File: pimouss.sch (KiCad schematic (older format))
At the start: 18 parts, among them J1 Conn_02x10_Odd_Even, J2 TMS-105-57-GD, J3 Conn_02x10_Odd_Even, P1 QSH-060-01-L-D-A, U1 SN74AUC1G19

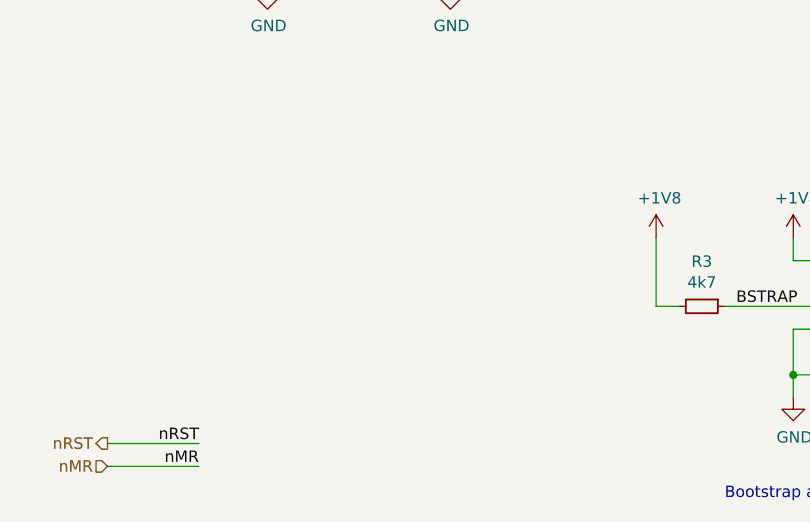
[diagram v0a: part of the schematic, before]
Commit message: sch, master: Add pimouss SoM component
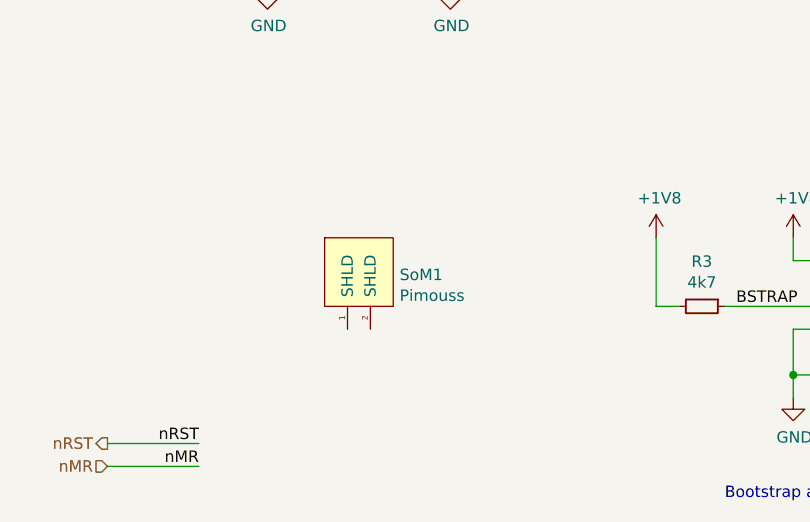
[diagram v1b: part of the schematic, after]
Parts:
- added SoM1: Pimouss, pimouss-motherboard:Pimouss, symbol pimouss-motherboard:Pimouss
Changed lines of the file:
@@
 	3000 1800 3400 1800
 Connection ~ 7100 4400
+$Comp
+L pimouss-motherboard:Pimouss SoM1
+U 1 1 5DBDBE10
+P 2450 5700
+F 0 "SoM1" H 2778 5538 50  0000 L CNN
+F 1 "Pimouss" H 2778 5447 50  0000 L CNN
+F 2 "pimouss-motherboard:Pimouss" H 2450 5700 50  0001 C CNN
+F 3 "" H 2450 5700 50  0001 C CNN
+	1    2450 5700
+	1    0    0    -1
+$EndComp
 $EndSCHEMATC

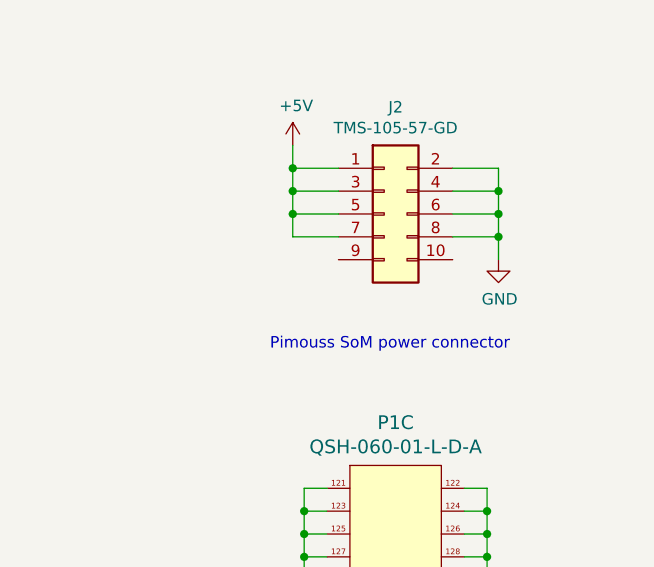
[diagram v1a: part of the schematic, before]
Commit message: lib: Finally fix TSM-105 symbol
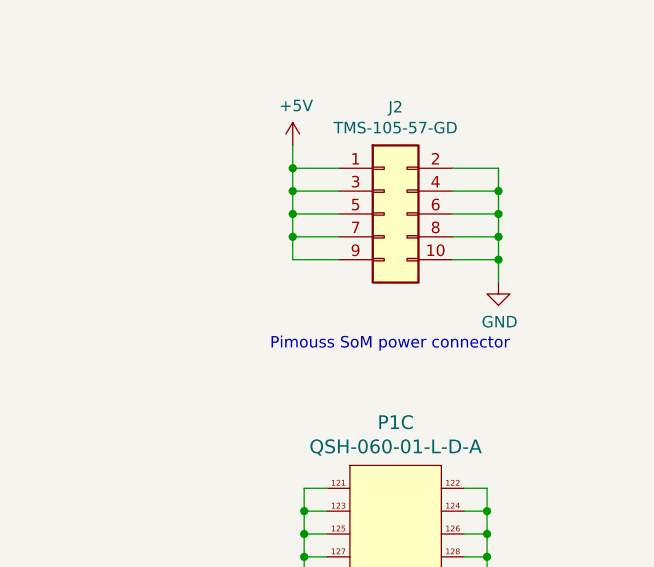
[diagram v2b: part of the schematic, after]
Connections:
- net +5V: now also J2.9 (Pin_9)
- net GND: now also J2.10 (Pin_10)
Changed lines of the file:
@@
 L power:GND #PWR025
 U 1 1 5DAB4CAB
-P 10350 2550
-F 0 "#PWR025" H 10350 2300 50  0001 C CNN
-F 1 "GND" H 10355 2377 50  0000 C CNN
-F 2 "" H 10350 2550 50  0001 C CNN
-F 3 "" H 10350 2550 50  0001 C CNN
-	1    10350 2550
+P 10350 2650
+F 0 "#PWR025" H 10350 2400 50  0001 C CNN
+F 1 "GND" H 10355 2477 50  0000 C CNN
+F 2 "" H 10350 2650 50  0001 C CNN
+F 3 "" H 10350 2650 50  0001 C CNN
+	1    10350 2650
 	1    0    0    -1
 $EndComp
@@
 	10150 2450 10350 2450
 Connection ~ 10350 2450
-Wire Wire Line
-	10350 2450 10350 2550
 Text Notes 10400 2950 2    50   ~ 0
 Pimouss SoM power connector
@@
 	1    0    0    -1
 $EndComp
+Wire Wire Line
+	10350 2450 10350 2550
+Wire Wire Line
+	10150 2550 10350 2550
+Connection ~ 10350 2550
+Wire Wire Line
+	10350 2550 10350 2650
+Wire Wire Line
+	9650 2550 9450 2550
+Wire Wire Line
+	9450 2550 9450 2450
+Connection ~ 9450 2450
 $EndSCHEMATC

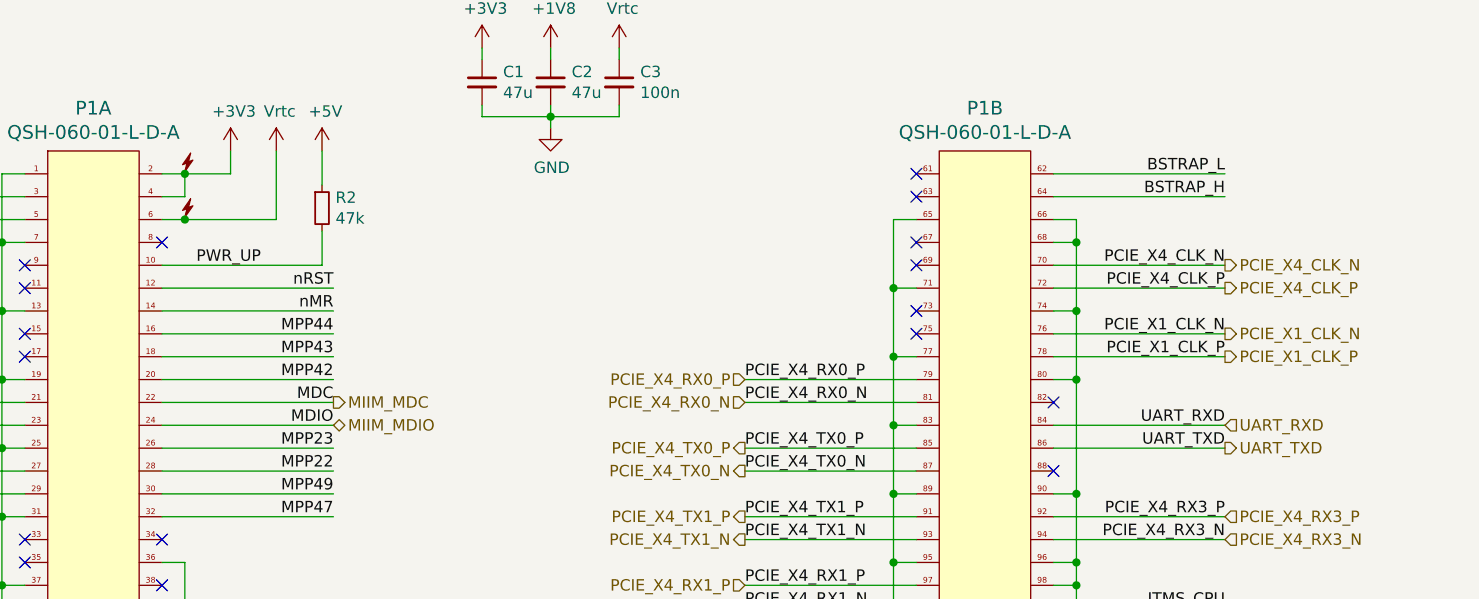
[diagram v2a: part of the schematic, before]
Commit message: sch, pcb: Add testpads on lots of signals
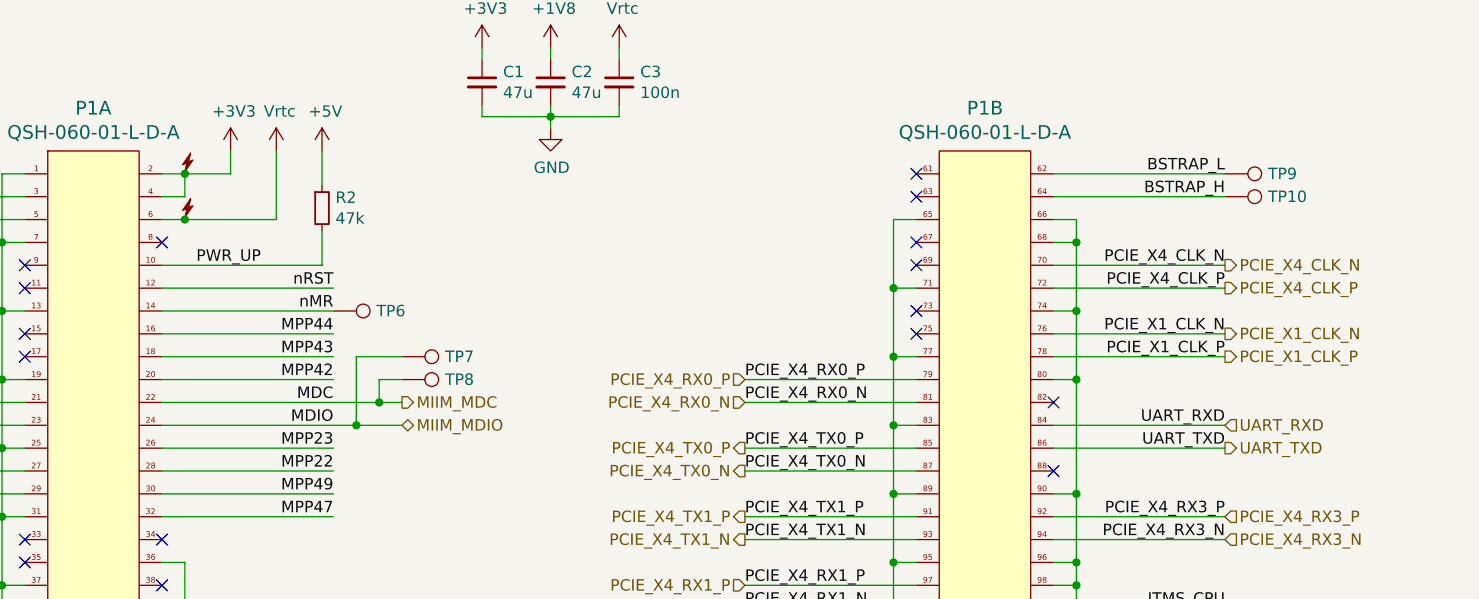
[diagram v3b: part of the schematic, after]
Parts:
- added TP10, TP6, TP7, TP8, TP9: TestPoint, TestPoint:TestPoint_Pad_D1.0mm, symbol Connector:TestPoint
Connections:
- net BSTRAP_H: now also TP10.1
- net BSTRAP_L: now also TP9.1
- net MIIM_MDC: now also TP8.1
- net MIIM_MDIO: now also TP7.1
- net nMR: now also TP6.1
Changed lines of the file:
@@
 PCIE_X4_RX3_N
-Wire Wire Line
-	3650 2600 2900 2600
-Wire Wire Line
-	3650 2700 2900 2700
 Wire Wire Line
 	3650 2100 2900 2100
@@
 NoConn ~ 6200 2200
 NoConn ~ 6200 2300
-Wire Wire Line
-	7550 1600 6800 1600
-Wire Wire Line
-	7550 1700 6800 1700
-Text Label 7550 1600 2    50   ~ 0
-BSTRAP_L
-Text Label 7550 1700 2    50   ~ 0
-BSTRAP_H
 NoConn ~ 6800 2900
 NoConn ~ 6800 2600
@@
 Text HLabel 3650 4500 2    50   BiDi ~ 0
 SD_D0
-Text HLabel 3650 2600 2    50   Output ~ 0
+Text HLabel 3950 2600 2    50   Output ~ 0
 MIIM_MDC
-Text HLabel 3650 2700 2    50   BiDi ~ 0
+Text HLabel 3950 2700 2    50   BiDi ~ 0
 MIIM_MDIO
 Text HLabel 1550 1800 0    50   Output ~ 0
@@
 	9450 2550 9450 2450
 Connection ~ 9450 2450
+$Comp
+L Connector:TestPoint TP?
+U 1 1 5D19D3D1
+P 3950 2400
+AR Path="/5D05A5E1/5D19D3D1" Ref="TP?"  Part="1"
+AR Path="/5CE77C37/5D19D3D1" Ref="TP7"  Part="1"
+F 0 "TP7" V 3950 2588 50  0000 L CNN
+F 1 "TestPoint" V 3995 2588 50  0001 L CNN
+F 2 "TestPoint:TestPoint_Pad_D1.0mm" H 4150 2400 50  0001 C CNN
+F 3 "~" H 4150 2400 50  0001 C CNN
+	1    3950 2400
+	0    1    1    0
+$EndComp
+$Comp
+L Connector:TestPoint TP?
+U 1 1 5D1B314D
+P 3950 2500
+AR Path="/5D05A5E1/5D1B314D" Ref="TP?"  Part="1"
+AR Path="/5CE77C37/5D1B314D" Ref="TP8"  Part="1"
+F 0 "TP8" V 3950 2688 50  0000 L CNN
+F 1 "TestPoint" V 3995 2688 50  0001 L CNN
+F 2 "TestPoint:TestPoint_Pad_D1.0mm" H 4150 2500 50  0001 C CNN
+F 3 "~" H 4150 2500 50  0001 C CNN
+	1    3950 2500
+	0    1    1    0
+$EndComp
+Wire Wire Line
+	2900 2600 3850 2600
+Wire Wire Line
+	2900 2700 3750 2700
+Wire Wire Line
+	3950 2500 3850 2500
+Wire Wire Line
+	3850 2500 3850 2600
+Connection ~ 3850 2600
+Wire Wire Line
+	3850 2600 3950 2600
+Wire Wire Line
+	3950 2400 3750 2400
+Wire Wire Line
+	3750 2400 3750 2700
+Connection ~ 3750 2700
+Wire Wire Line
+	3750 2700 3950 2700
+Text Label 7550 1700 2    50   ~ 0
+BSTRAP_H
+Text Label 7550 1600 2    50   ~ 0
+BSTRAP_L
+Wire Wire Line
+	7550 1600 6800 1600
+Wire Wire Line
+	7550 1700 6800 1700
+$Comp
+L Connector:TestPoint TP?
+U 1 1 5D2A7F76
+P 7550 1600
+AR Path="/5D05A5E1/5D2A7F76" Ref="TP?"  Part="1"
+AR Path="/5CE77C37/5D2A7F76" Ref="TP9"  Part="1"
+F 0 "TP9" V 7550 1788 50  0000 L CNN
+F 1 "TestPoint" V 7595 1788 50  0001 L CNN
+F 2 "TestPoint:TestPoint_Pad_D1.0mm" H 7750 1600 50  0001 C CNN
+F 3 "~" H 7750 1600 50  0001 C CNN
+	1    7550 1600
+	0    1    1    0
+$EndComp
+$Comp
+L Connector:TestPoint TP?
+U 1 1 5D2A76E3
+P 7550 1700
+AR Path="/5D05A5E1/5D2A76E3" Ref="TP?"  Part="1"
+AR Path="/5CE77C37/5D2A76E3" Ref="TP10"  Part="1"
+F 0 "TP10" V 7550 1888 50  0000 L CNN
+F 1 "TestPoint" V 7595 1888 50  0001 L CNN
+F 2 "TestPoint:TestPoint_Pad_D1.0mm" H 7750 1700 50  0001 C CNN
+F 3 "~" H 7750 1700 50  0001 C CNN
+	1    7550 1700
+	0    1    1    0
+$EndComp
+$Comp
+L Connector:TestPoint TP?
+U 1 1 5D3350DF
+P 3650 2200
+AR Path="/5D05A5E1/5D3350DF" Ref="TP?"  Part="1"
+AR Path="/5CE77C37/5D3350DF" Ref="TP6"  Part="1"
+F 0 "TP6" V 3650 2388 50  0000 L CNN
+F 1 "TestPoint" V 3695 2388 50  0001 L CNN
+F 2 "TestPoint:TestPoint_Pad_D1.0mm" H 3850 2200 50  0001 C CNN
+F 3 "~" H 3850 2200 50  0001 C CNN
+	1    3650 2200
+	0    1    1    0
+$EndComp
 $EndSCHEMATC

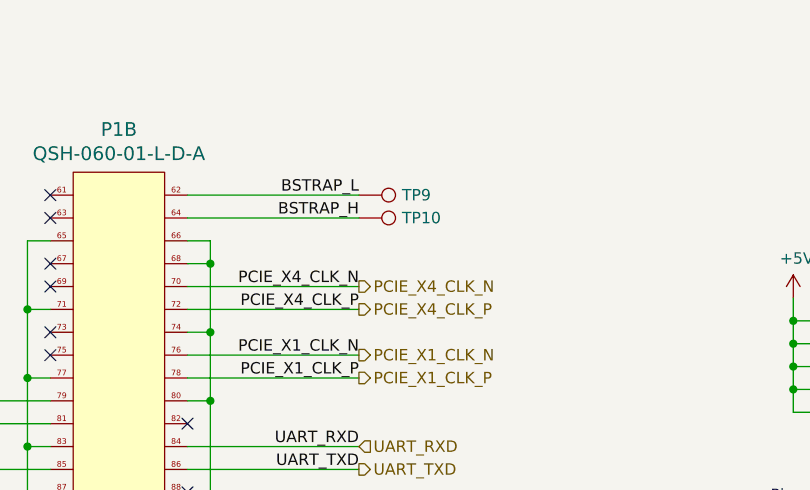
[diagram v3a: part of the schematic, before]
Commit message: sch: Remove BSTRAP_H/L test pads
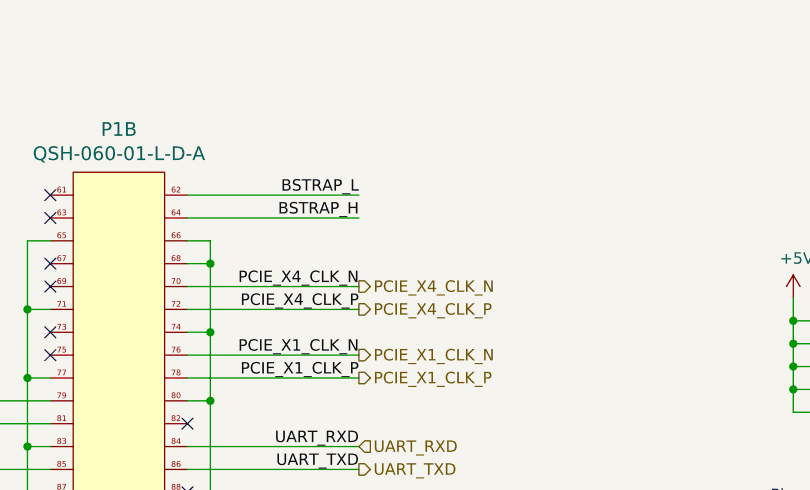
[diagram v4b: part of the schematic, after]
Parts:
- removed TP10, TP9: TestPoint, TestPoint:TestPoint_Pad_D1.0mm, symbol Connector:TestPoint
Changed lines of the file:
@@
-$Comp
-L Connector:TestPoint TP?
-U 1 1 5D2A7F76
-P 7550 1600
-AR Path="/5D05A5E1/5D2A7F76" Ref="TP?"  Part="1"
-AR Path="/5CE77C37/5D2A7F76" Ref="TP9"  Part="1"
-F 0 "TP9" V 7550 1788 50  0000 L CNN
-F 1 "TestPoint" V 7595 1788 50  0001 L CNN
-F 2 "TestPoint:TestPoint_Pad_D1.0mm" H 7750 1600 50  0001 C CNN
-F 3 "~" H 7750 1600 50  0001 C CNN
-	1    7550 1600
-	0    1    1    0
-$EndComp
-$Comp
-L Connector:TestPoint TP?
-U 1 1 5D2A76E3
-P 7550 1700
-AR Path="/5D05A5E1/5D2A76E3" Ref="TP?"  Part="1"
-AR Path="/5CE77C37/5D2A76E3" Ref="TP10"  Part="1"
-F 0 "TP10" V 7550 1888 50  0000 L CNN
-F 1 "TestPoint" V 7595 1888 50  0001 L CNN
-F 2 "TestPoint:TestPoint_Pad_D1.0mm" H 7750 1700 50  0001 C CNN
-F 3 "~" H 7750 1700 50  0001 C CNN
-	1    7550 1700
-	0    1    1    0
-$EndComp
 $Comp
 L Connector:TestPoint TP?

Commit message: sch, pcb: Replace CH340 with FT230 and add USB host port
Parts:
- added P6: USB-C-2.0-FEMALE, pimouss-motherboard:USB-C-FEMALE, symbol pimouss-motherboard:USB-C-2.0-FEMALE
- added R82, R83: 56k, Resistor_SMD:R_0603_1608Metric, symbol Device:R_Small
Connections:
- net +5V: now also P6.A4 (VBUS), P6.A9 (VBUS), P6.B4 (VBUS), P6.B9 (VBUS), R82.2, R83.2
- net GND: now also P6.A1 (GND), P6.A12 (GND), P6.B1 (GND), P6.B12 (GND), P6.S1 (SHIELD), P6.S2 (SHIELD), P6.S3 (SHIELD), P6.S4 (SHIELD)
- net USB_HOST_N: now reaches P1.38
- net USB_HOST_N: now also P6.A7 (D-), P6.B7 (D-)
- net USB_HOST_P: now reaches P1.40
- net USB_HOST_P: now also P6.A6 (D+), P6.B6 (D+)
- new net: P6.A5 (CC1), R82.1
- new net: P6.B5 (CC2), R83.1
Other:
- moved on the sheet: J2, P1C

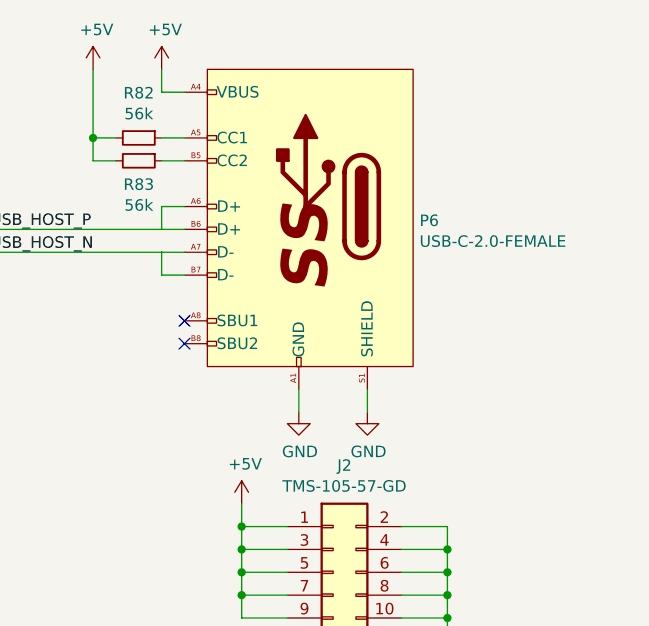
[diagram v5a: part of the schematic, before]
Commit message: sch, pcb: Replace USB-C connectors with vertical ones
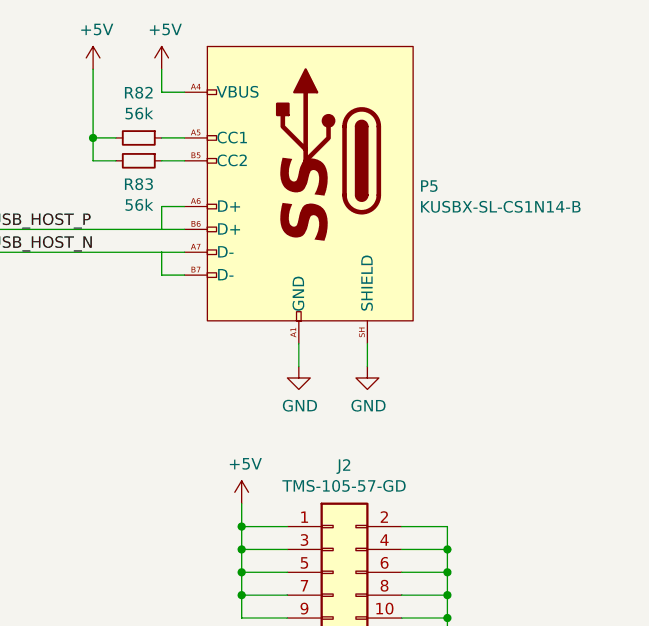
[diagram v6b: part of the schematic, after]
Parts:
- removed P6: USB-C-2.0-FEMALE, pimouss-motherboard:USB-C-FEMALE, symbol pimouss-motherboard:USB-C-2.0-FEMALE
- added P5: KUSBX-SL-CS1N14-B, pimouss-motherboard:KUSBX-SL-CS1N14-B, symbol pimouss-motherboard:KUSBX-SL-CS1N14-B
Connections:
- net +5V: now also P5.A4 (VBUS), P5.A9 (VBUS), P5.B4 (VBUS), P5.B9 (VBUS)
- net GND: now also P5.A1 (GND), P5.A12 (GND), P5.B1 (GND), P5.B12 (GND), P5.SH (SHIELD)
- net USB_HOST_N: now also P5.A7 (D-), P5.B7 (D-)
- net USB_HOST_P: now also P5.A6 (D+), P5.B6 (D+)
- net at R82.1: now also P5.A5 (CC1)
- net at R83.1: now also P5.B5 (CC2)
- no-connect marks 28 -> 26
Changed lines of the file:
@@
 Text Label 3650 3500 2    50   ~ 0
 USB_HOST_P
-$Comp
-L pimouss-motherboard:USB-C-2.0-FEMALE P6
-U 1 1 5DDF3054
-P 10400 750
-F 0 "P6" H 10372 88  50  0000 R CNN
-F 1 "USB-C-2.0-FEMALE" H 10372 -3  50  0000 R CNN
-F 2 "pimouss-motherboard:USB-C-FEMALE" H 11150 -750 50  0001 C CNN
-F 3 "https://www.usb.org/sites/default/files/documents/usb_type-c.zip" H 11050 250 50  0001 C CNN
-	1    10400 750
-	-1   0    0    -1
-$EndComp
 Text Label 1900 6700 2    50   ~ 0
 nMR
@@
 L power:GND #PWR0160
 U 1 1 5DED3B57
-P 9900 2250
-F 0 "#PWR0160" H 9900 2000 50  0001 C CNN
-F 1 "GND" H 9905 2077 50  0000 C CNN
-F 2 "" H 9900 2250 50  0001 C CNN
-F 3 "" H 9900 2250 50  0001 C CNN
-	1    9900 2250
+P 9900 2050
+F 0 "#PWR0160" H 9900 1800 50  0001 C CNN
+F 1 "GND" H 9905 1877 50  0000 C CNN
+F 2 "" H 9900 2050 50  0001 C CNN
+F 3 "" H 9900 2050 50  0001 C CNN
+	1    9900 2050
 	1    0    0    -1
 $EndComp
@@
 L power:GND #PWR0195
 U 1 1 5DED4037
-P 10200 2250
-F 0 "#PWR0195" H 10200 2000 50  0001 C CNN
-F 1 "GND" H 10205 2077 50  0000 C CNN
-F 2 "" H 10200 2250 50  0001 C CNN
-F 3 "" H 10200 2250 50  0001 C CNN
-	1    10200 2250
+P 10200 2050
+F 0 "#PWR0195" H 10200 1800 50  0001 C CNN
+F 1 "GND" H 10205 1877 50  0000 C CNN
+F 2 "" H 10200 2050 50  0001 C CNN
+F 3 "" H 10200 2050 50  0001 C CNN
+	1    10200 2050
 	1    0    0    -1
 $EndComp
-NoConn ~ 9400 1950
-NoConn ~ 9400 1850
 $Comp
 L power:+5V #PWR0198
@@
 $EndComp
 Wire Wire Line
-	9900 2150 9900 2250
+	9900 1950 9900 2050
 Wire Wire Line
-	10200 2150 10200 2250
+	10200 1950 10200 2050
+$Comp
+L pimouss-motherboard:KUSBX-SL-CS1N14-B P5
+U 1 1 5DEF3C25
+P 10400 650
+F 0 "P5" H 10372 38  50  0000 R CNN
+F 1 "KUSBX-SL-CS1N14-B" H 10372 -53 50  0000 R CNN
+F 2 "pimouss-motherboard:KUSBX-SL-CS1N14-B" H 11150 -750 50  0001 C CNN
+F 3 "https://www.usb.org/sites/default/files/documents/usb_type-c.zip" H 11050 250 50  0001 C CNN
+	1    10400 650
+	-1   0    0    -1
+$EndComp
 $EndSCHEMATC

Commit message: sch, pcb: Replace large JTAG headers with 1.27 ones
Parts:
- J3: footprint Connector_PinHeader_2.54mm:PinHeader_2x10_P2.54mm_Vertical -> Connector_PinHeader_1.27mm:PinHeader_2x10_P1.27mm_Vertical_SMD
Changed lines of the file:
@@
 F 0 "J3" H 10300 6217 50  0000 C CNN
 F 1 "Conn_02x10_Odd_Even" H 10300 6126 50  0000 C CNN
-F 2 "Connector_PinHeader_2.54mm:PinHeader_2x10_P2.54mm_Vertical" H 10250 5600 50  0001 C CNN
+F 2 "Connector_PinHeader_1.27mm:PinHeader_2x10_P1.27mm_Vertical_SMD" H 10250 5600 50  0001 C CNN
 F 3 "~" H 10250 5600 50  0001 C CNN
 	1    10250 5600
